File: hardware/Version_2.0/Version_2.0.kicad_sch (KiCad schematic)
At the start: 49 parts, among them J1 Conn_Coaxial, J2 Conn_Coaxial, J3 Conn_01x06_Pin, J4 Conn_01x06_Pin, J5 Conn_Coaxial, U1 ADF4351, Y1 SG-5032CAN

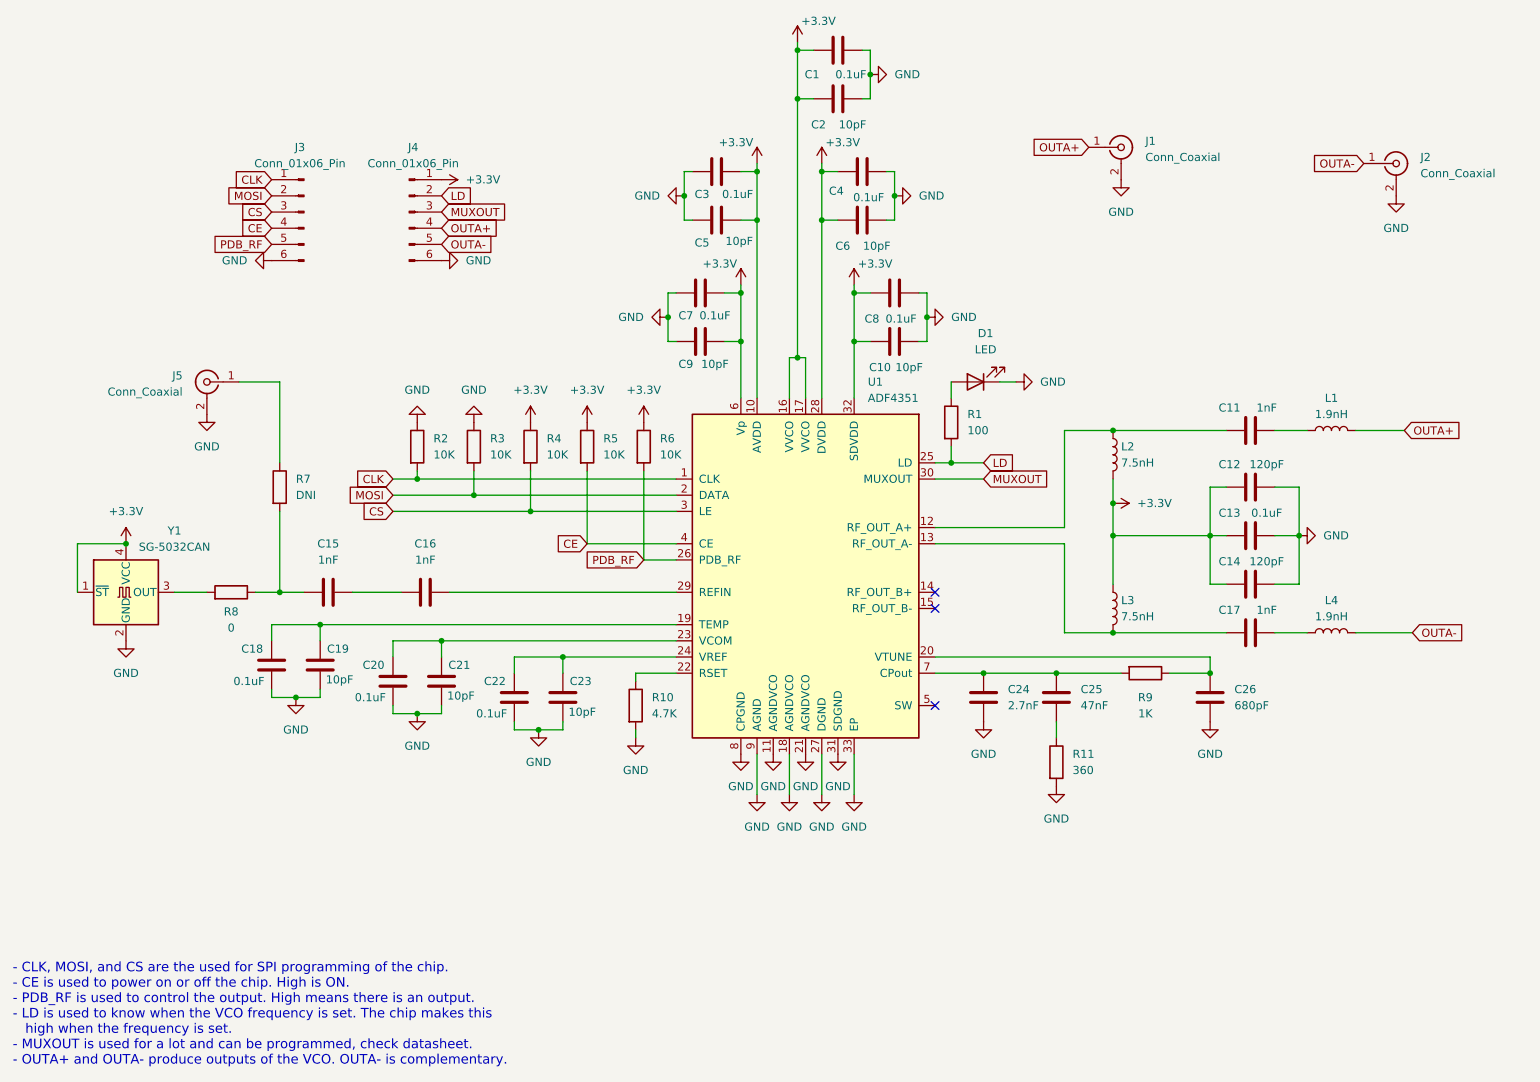
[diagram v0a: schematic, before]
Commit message: completed version 2 and version 3 pcb and production files completed
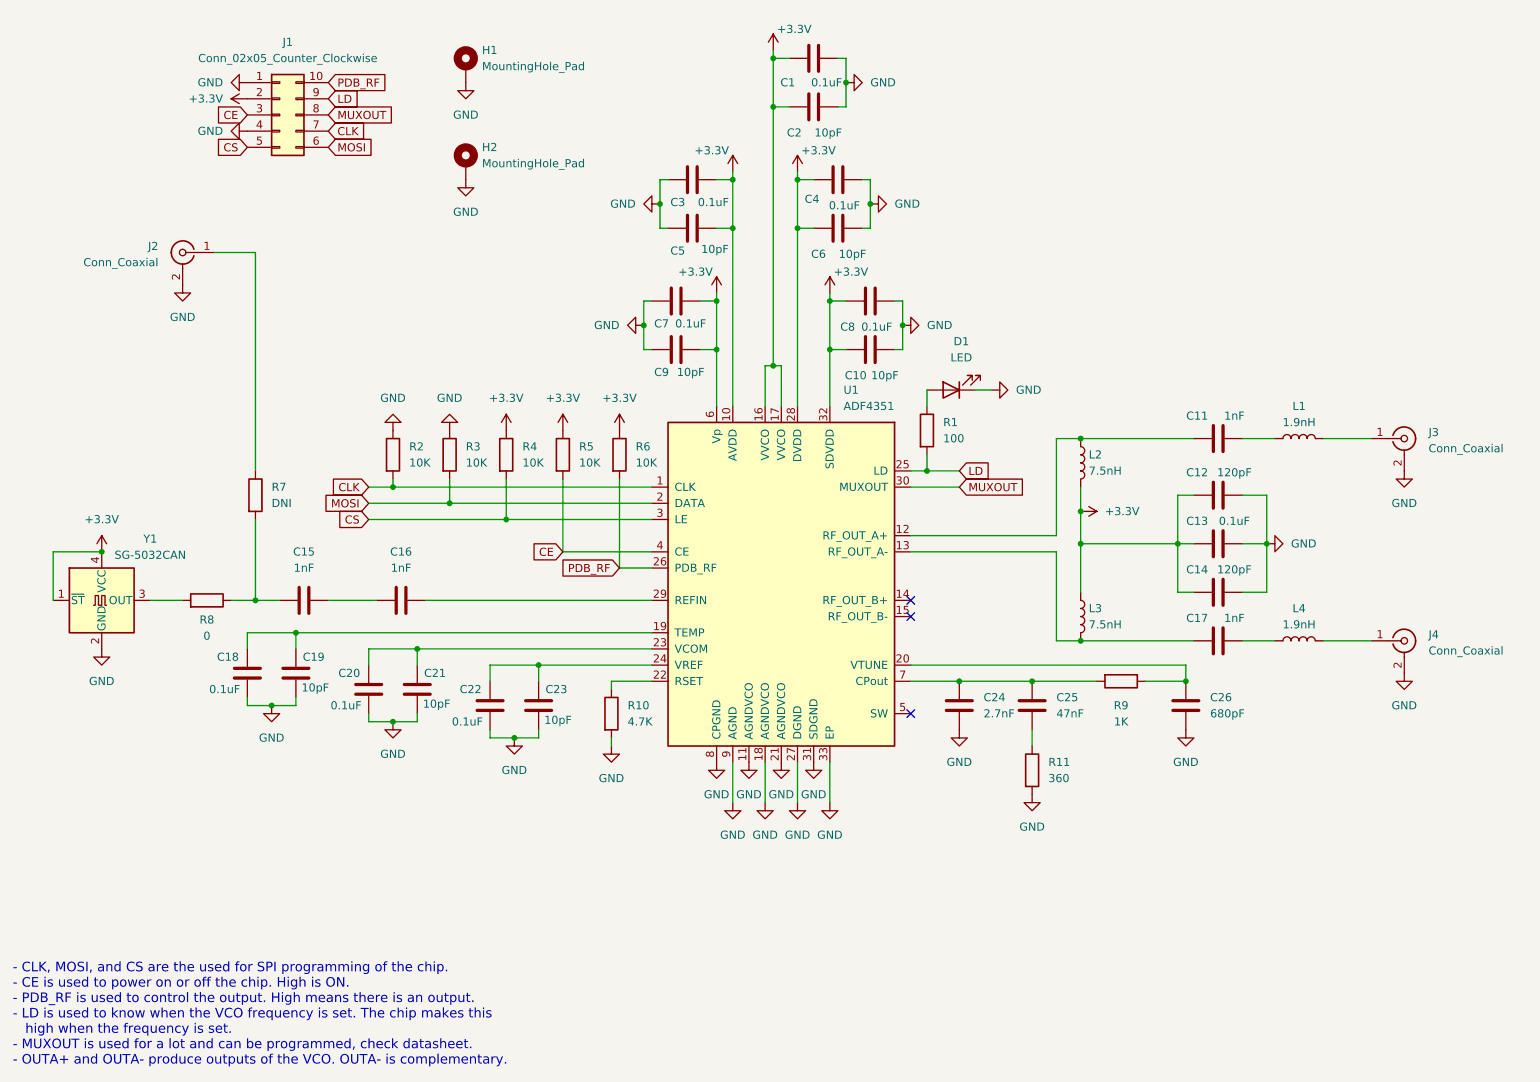
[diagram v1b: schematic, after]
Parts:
- removed J1, J5: Conn_Coaxial, Connector_Coaxial:SMA_Molex_73251-1153_EdgeMount_Horizontal, symbol Connector:Conn_Coaxial
- removed J3, J4: Conn_01x06_Pin, Connector_PinSocket_2.54mm:PinSocket_1x06_P2.54mm_Vertical, symbol Connector:Conn_01x06_Pin
- added H1, H2: MountingHole_Pad, MountingHole:MountingHole_3.2mm_M3_Pad, symbol Mechanical:MountingHole_Pad
- added J1: Conn_02x05_Counter_Clockwise, Connector_PinHeader_2.54mm:PinHeader_2x05_P2.54mm_Vertical, symbol Connector_Generic:Conn_02x05_Counter_Clockwise
- added J3, J4: Conn_Coaxial, Connector_Coaxial:SMA_Molex_73251-1153_EdgeMount_Horizontal, symbol Connector:Conn_Coaxial
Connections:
- net +3.3V: now also J1.2 (Pin_2)
- net CE: now also J1.3 (Pin_3)
- net CLK: now also J1.7 (Pin_7)
- net CS: now also J1.5 (Pin_5)
- net GND: now also H1.1, H2.1, J1.1 (Pin_1), J1.4 (Pin_4), J3.2 (Ext), J4.2 (Ext)
- net LD: now also J1.9 (Pin_9)
- net MOSI: now also J1.6 (Pin_6)
- net MUXOUT: now also J1.8 (Pin_8)
- net PDB_RF: now also J1.10 (Pin_10)
- net at R7.1: now also J2.1 (In)
- net OUTA+: no longer names the net of L1.2
- net OUTA+: now also J3.1 (In)
- net OUTA-: no longer names the net of L4.2
- net OUTA-: now also J4.1 (In); no longer J2.1 (In)
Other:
- title: ADF4351 Trial Board -> ADF4351
